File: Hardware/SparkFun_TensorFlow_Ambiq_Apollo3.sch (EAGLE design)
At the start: 67 parts, among them J5 CORTEX_DEBUG, J7 CAMERA-HIMAX, U2 LIS2DH12, U3 1.8V, U5 ARTEMIS_MODULESMD, Y2 32.768kHz

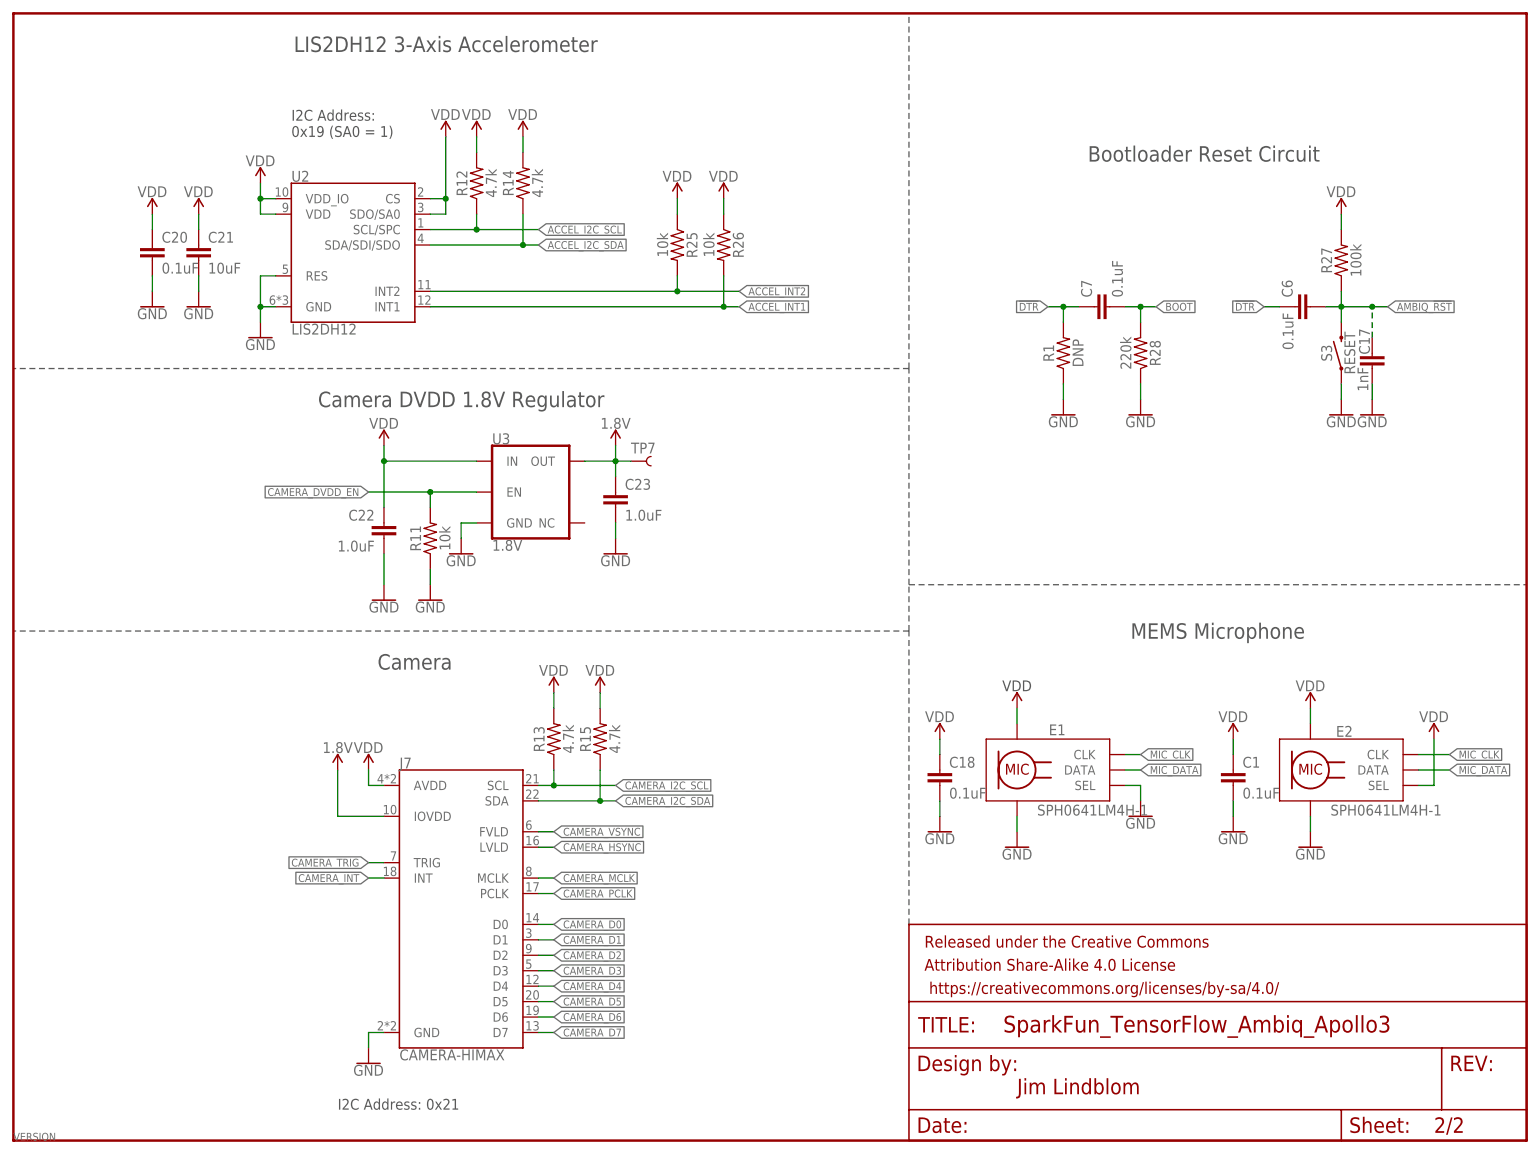
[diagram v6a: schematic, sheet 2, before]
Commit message: Add power control via GPIO to accel and mics.
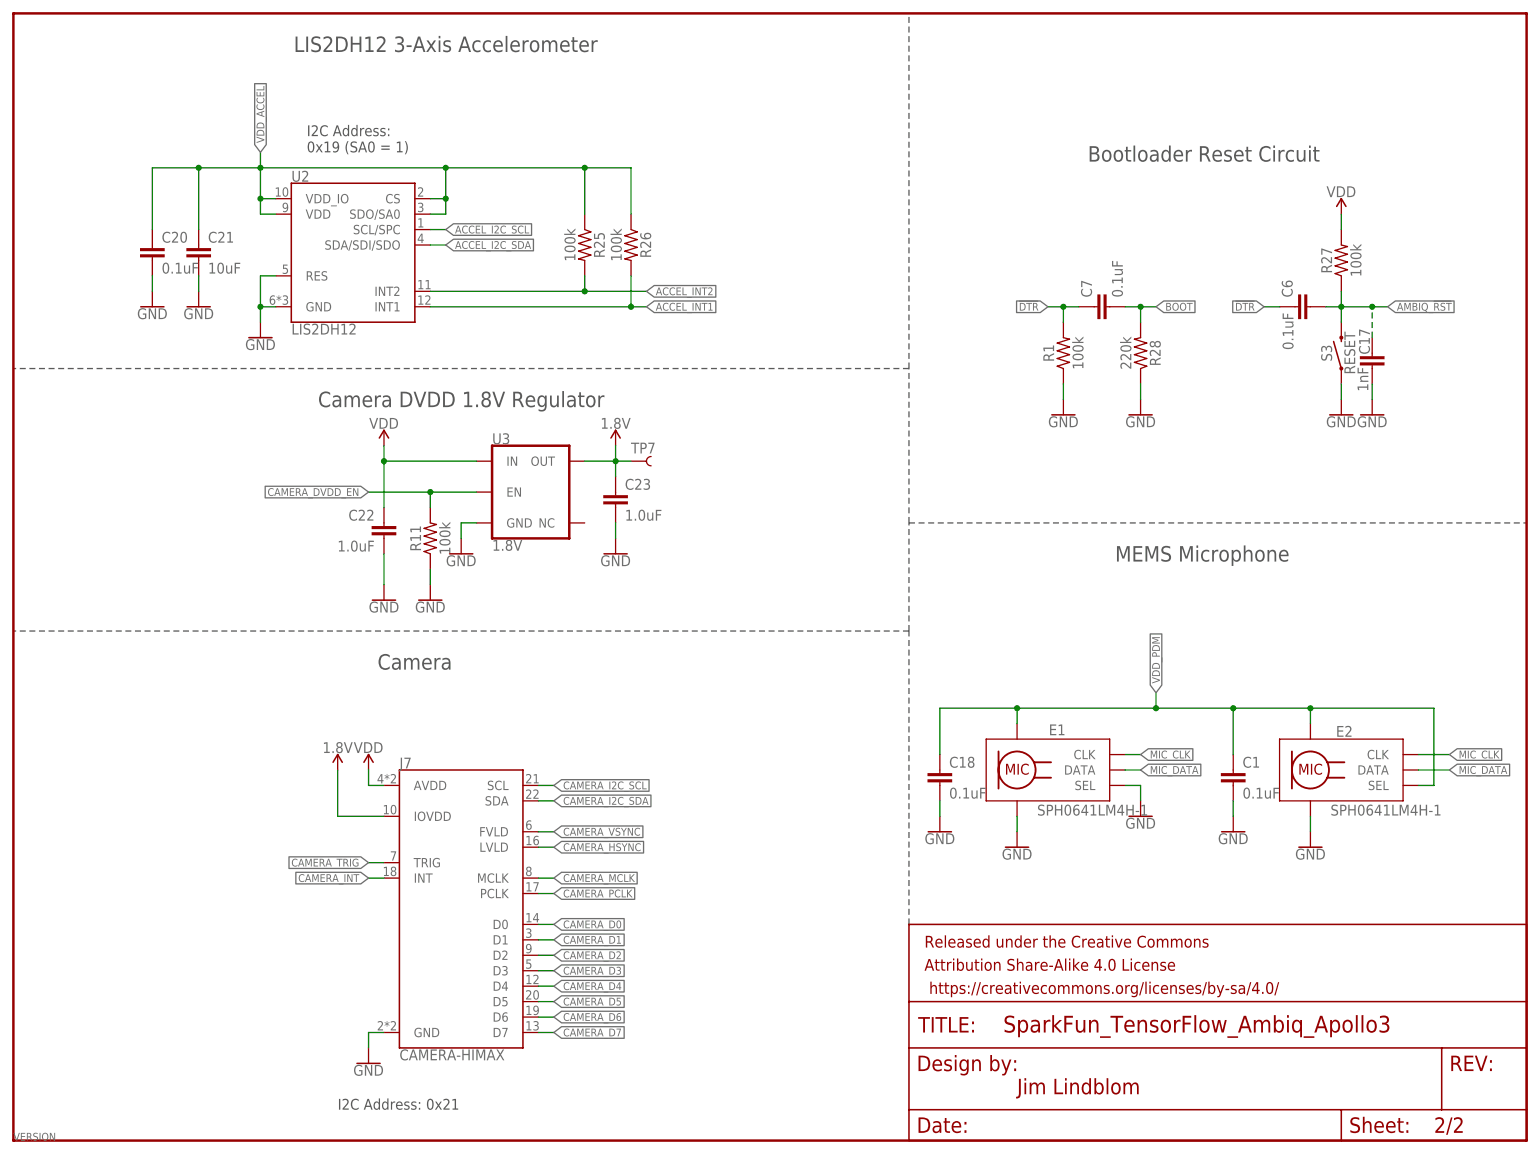
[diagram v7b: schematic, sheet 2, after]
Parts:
- removed R12, R13, R14, R15: 4.7k, SparkFun-Resistors:4.7KOHM-0603-1/10W-1%
- added JP1: JUMPER-COMBO_2_NC_TRACE, SparkFun-Jumpers:JUMPER-COMBO_2_NC_TRACE
- R1: value DNP -> 100k
- R11, R25, R26: value 10k -> 100k; device SparkFun-Resistors:10KOHM-0402T-1/16W-1% -> SparkFun-Resistors:100KOHM-0402T-1/16W-1%
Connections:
- new net VDD_ACCEL: C20.1, C21.1, R25.1, R26.1, U2.CS, U2.SDO/SA0, U2.VDD, U2.VDD_IO, U5.(BLEIF_IRQ/SWO/I2SWCLK)D41
- new net VDD_PDM: C1.1, C18.1, E1.VDD, E2.SEL, E2.VDD, U5.(SLSCK/SLSCL/CLKOUT)D0
- new net VIN1: D1.C, D2.C, JP1.1
- net ACCEL_I2C_SCL: no longer R12.1
- net ACCEL_I2C_SDA: no longer R14.1
- net ACCEL_INT1: now also U5.(SLMISO)D2
- net ACCEL_INT2: now also U5.(SLMOSI/SLSDA)D1
- net CAMERA_I2C_SCL: no longer R13.1
- net CAMERA_I2C_SDA: no longer R15.1
- net VDD: now also JP1.2; no longer C1.1, C18.1, C20.1, C21.1, D1.C, D2.C, E1.VDD, E2.SEL, E2.VDD, R12.2, R13.2, R14.2, R15.2, R25.1, R26.1, U2.CS, U2.SDO/SA0, U2.VDD, U2.VDD_IO
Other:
- moved on the sheet: C11, C2, C4, R25, R26

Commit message: Change part ID on 0.1uF on bootload circuit
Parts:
- C7: device SparkFun-Capacitors:0.1UF-0603-25V-(+80/-20%) -> SparkFun-Capacitors:0.1UF-0603-25V-5%
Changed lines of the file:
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@@
 <?xml version="1.0" encoding="utf-8"?>
 <!DOCTYPE eagle SYSTEM "eagle.dtd">
-<eagle version="9.5.0">
+<eagle version="9.5.1">
 <drawing>
 <settings>
@@
 <part name="GND5" library="SparkFun-PowerSymbols" deviceset="GND" device=""/>
 <part name="R28" library="SparkFun-Resistors" deviceset="220KOHM" device="-0603-1/10W-1%" value="220k"/>
-<part name="C7" library="SparkFun-Capacitors" deviceset="0.1UF" device="-0603-25V-(+80/-20%)" value="0.1uF"/>
+<part name="C7" library="SparkFun-Capacitors" deviceset="0.1UF" device="-0603-25V-5%" value="0.1uF"/>
 <part name="C17" library="SparkFun-Capacitors" deviceset="1.0NF/1000PF" device="-0603-50V-10%" value="1nF"/>
 <part name="GND45" library="SparkFun-PowerSymbols" deviceset="GND" device=""/>
